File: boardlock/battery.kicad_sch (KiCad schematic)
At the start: 4 parts, among them U4 BQ27441DRZR-G1A, U5 BQ24075RGT

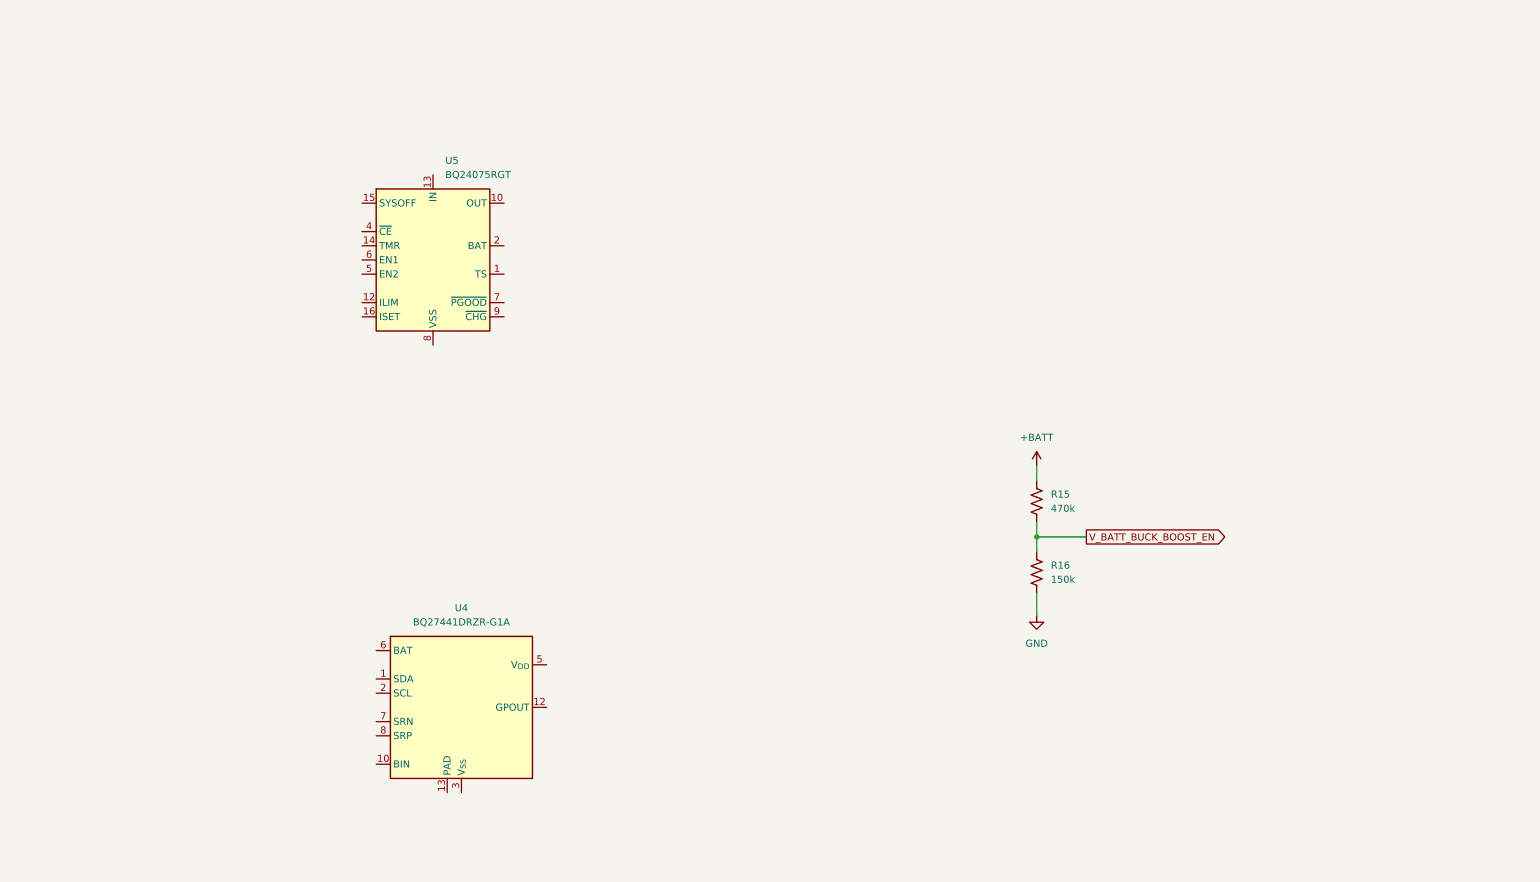
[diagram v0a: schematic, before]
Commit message: Started adding topology for batt charger
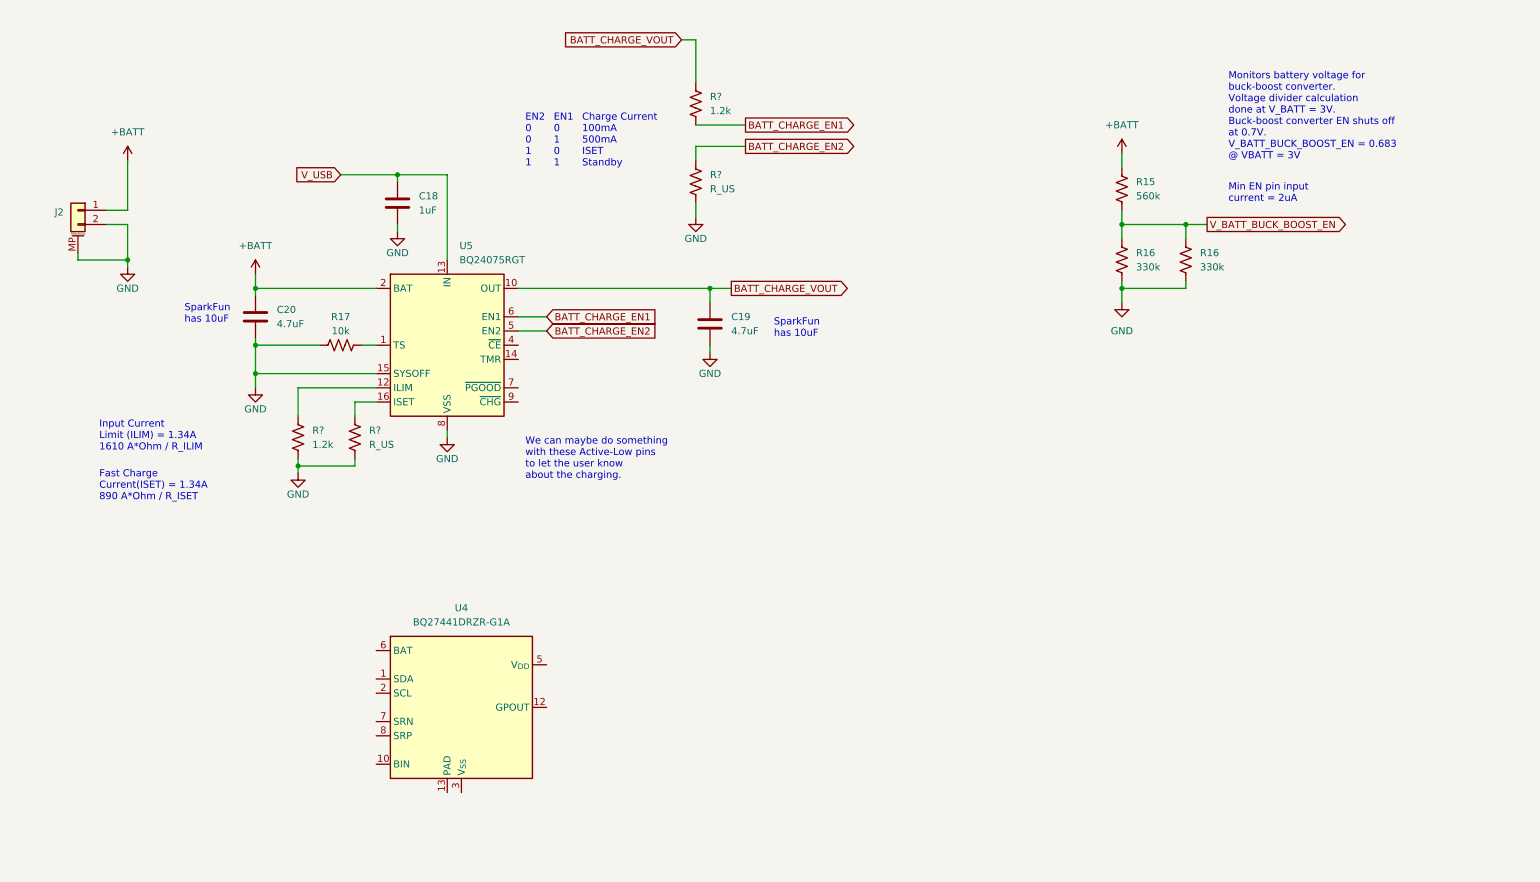
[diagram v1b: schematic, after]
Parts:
- added C18: 1uF, symbol Device:C
- added C19, C20: 4.7uF, symbol Device:C
- added J2: Conn_01x02_MountingPin, symbol Connector_Generic_MountingPin:Conn_01x02_MountingPin
- added R16: 330k, symbol Device:R_US
- added R17: 10k, symbol Device:R_US
- added R? (x2): R_US, symbol Device:R_US
- added R? (x2): 1.2k, symbol Device:R_US
- R15: value 470k -> 560k
- R16: value 150k -> 330k
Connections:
- net +BATT: now also U5.2 (BAT), U5.3 (BAT), C20.1, J2.1 (Pin_1)
- net GND: now also U5.15 (SYSOFF), U5.17 (VSS), U5.8 (VSS), C18.2, C19.2, C20.2, J2.2 (Pin_2), J2.MP (MountPin), R16.2, R17.1, R?.2, R?.2, R?.2
- net V_BATT_BUCK_BOOST_EN: now also R16.1
- net at U5.1 (TS): now also R17.2
- net BATT_CHARGE_VOUT: now reaches U5.10 (OUT), U5.11 (OUT)
- net BATT_CHARGE_VOUT: now also C19.1, R?.1
- net at U5.12 (ILIM): now also R?.1
- net V_USB: now reaches U5.13 (IN)
- net V_USB: now also C18.1
- net at U5.16 (ISET): now also R?.1
- net BATT_CHARGE_EN2: now reaches U5.5 (EN2)
- net BATT_CHARGE_EN2: now also R?.1
- net BATT_CHARGE_EN1: now reaches U5.6 (EN1)
- net BATT_CHARGE_EN1: now also R?.2
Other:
- note added: "Charge Current 100mA 500mA ISET Standby"
- note added: "EN1 0 1 0 1"
- note added: "EN2 0 0 1 1"
- note added: "Fast Charge Current(ISET) = 1.34A 890 A*Ohm / R_ISET"
- note added: "Input Current Limit (ILIM) = 1.34A 1610 A*Ohm / R_ILIM"
- note added: "Min EN pin input current = 2uA"
- note added: "Monitors battery voltage for buck-boost converter. Voltage divider calculation done at V_BATT = 3V. Buck-boost converter EN shuts off at 0.7V. V_BATT_BUCK_BOOST_EN = 0.683 @ VBATT = 3V"
- note added: "SparkFun has 10uF"
- note added: "We can maybe do something with these Active-Low pins to let the user know about the charging."
- moved on the sheet: R15, R16, U5

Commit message: edited battery management
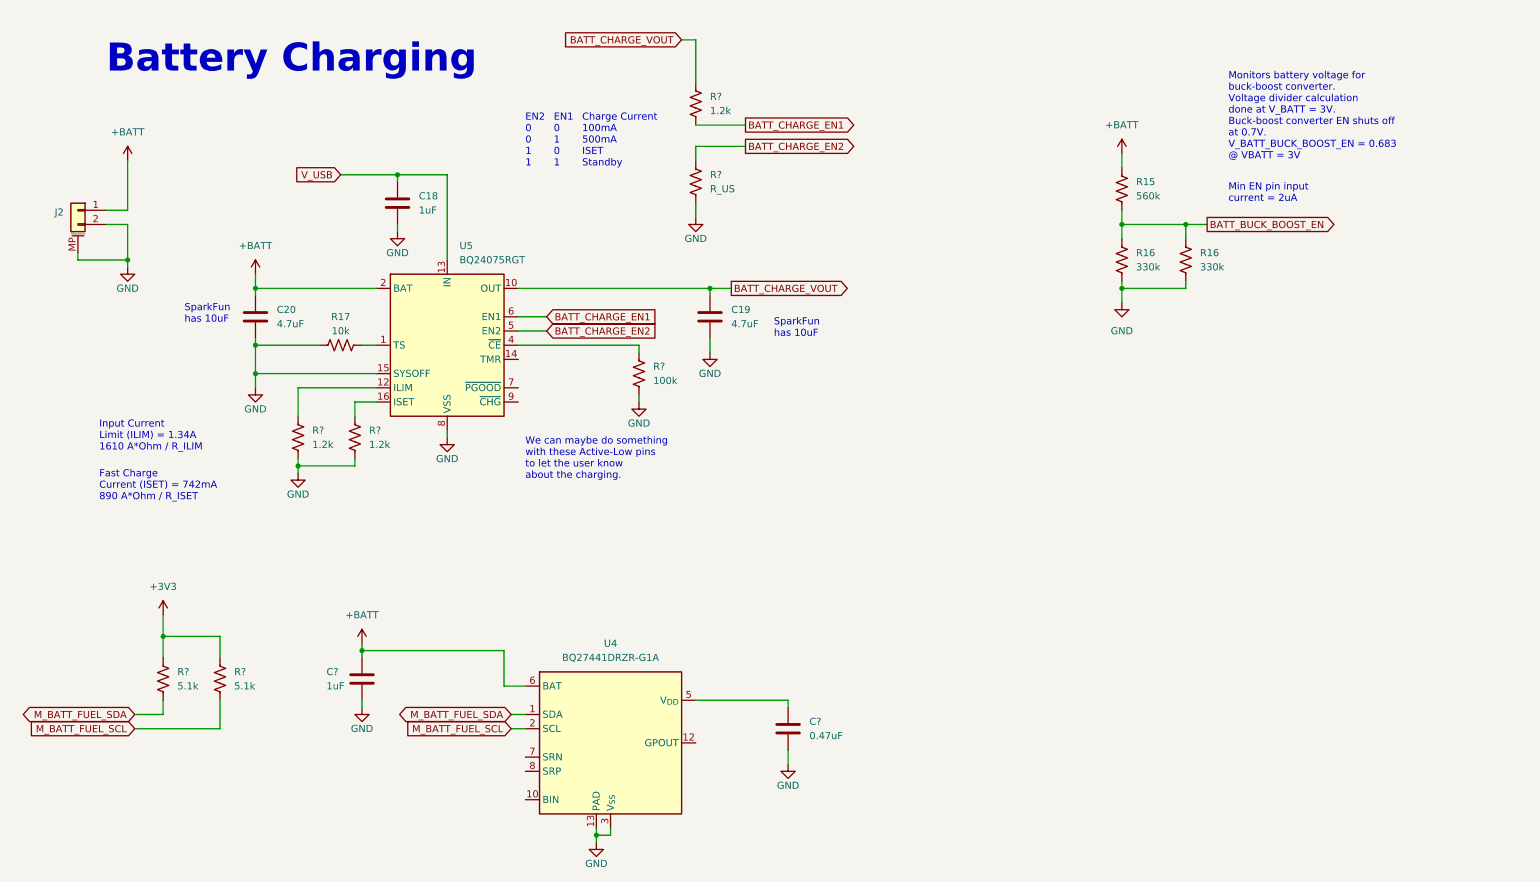
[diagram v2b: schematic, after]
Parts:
- added C?: 0.47uF, symbol Device:C
- added C?: 1uF, symbol Device:C
- added R? (x2): 5.1k, symbol Device:R_US
- added R?: 100k, symbol Device:R_US
- R?: value R_US -> 1.2k
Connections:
- net +BATT: now also U4.6 (BAT), C?.1
- net GND: now also U4.13 (PAD), U4.3 (V_{SS}), C?.2, C?.2, R?.2
- net at U5.4 (~{CE}): now also R?.1
- net M_BATT_FUEL_SDA: now reaches U4.1 (SDA)
- net M_BATT_FUEL_SDA: now also R?.2
- net M_BATT_FUEL_SCL: now reaches U4.2 (SCL)
- net M_BATT_FUEL_SCL: now also R?.2
- net at U4.5 (V_{DD}): now also C?.1
- net V_BATT_BUCK_BOOST_EN renamed BATT_BUCK_BOOST_EN
- new net +3V3: R?.1, R?.1
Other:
- note added: "Battery Charging"
- note added: "Fast Charge Current (ISET) = 742mA 890 A*Ohm / R_ISET"
- note removed: "Fast Charge Current(ISET) = 1.34A 890 A*Ohm / R_ISET"
- moved on the sheet: C19, U4

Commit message: Zecong edits
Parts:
- removed R15: 560k, symbol Device:R_US
- removed R16 (x2): 330k, symbol Device:R_US
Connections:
- net BATT_CHARGE_N_PGOOD: now reaches U5.7 (~{PGOOD})
- net BATT_CHARGE_N_CHG: now reaches U5.9 (~{CHG})
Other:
- note removed: "Min EN pin input current = 2uA"
- note removed: "Monitors battery voltage for buck-boost converter. Voltage divider calculation done at V_BATT = 3V. Buck-boost converter EN shuts off at 0.7V. V_BATT_BUCK_BOOST_EN = 0.683 @ VBATT = 3V"
- moved on the sheet: C?, R?

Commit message: More zecong edits
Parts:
- removed R17: 10k, symbol Device:R_US
- removed R? (x2): 5.1k, symbol Device:R_US
- added R?: 10k, symbol Device:R_US
- added R? (x2): 5.1k, symbol Device:R_US
- added R?: 47k, symbol Device:R_US
- added R?: R_US, symbol Device:R_US
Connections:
- net +3V3: now also R?.1, R?.1
- net +BATT: now also U4.7 (SRN), U4.8 (SRP), R?.1, R?.2
- net GND: now also R?.2, R?.2
- net TS_RESISTOR: now reaches U5.1 (TS)
- net TS_RESISTOR: now also U4.10 (BIN), R?.1
- net at U5.14 (TMR): now also R?.1
- net BATT_CHARGE_N_CHG renamed M_BATT_CHARGE_N_CHG
- net M_BATT_CHARGE_N_CHG: now also R?.2
- net BATT_CHARGE_N_PGOOD renamed M_BATT_CHARGE_N_PGOOD
- net M_BATT_CHARGE_N_PGOOD: now also R?.2
- net M_BATT_FUEL_SCL renamed M_I2C_SCL
- net M_BATT_FUEL_SDA renamed M_I2C_SDA
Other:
- note added: "10k Resistor used in place of 10k NTC thermistor of the battery pack"
- note added: "Need to have connector with BATTERY_IN. This is the input to the shunt resistor. VBATT is the actual battery voltage we want to work with. No sweat on the shunt resistor value. Max voltage drop is 20mV."
- company: (none) -> Schetmatic
- title: (none) -> BoardLock Schematic
- moved on the sheet: C19, C?, R?

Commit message: finishing touches
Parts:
- removed R?: R_US, symbol Device:R_US
- added R?: R_US, symbol Device:R_US
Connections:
- net +BATT: now also R?.1; no longer C?.1, U4.6 (BAT), U4.8 (SRP)
- net M_FUEL_GPOUT: now reaches U4.12 (GPOUT)
- new net BATTERY_IN: C?.1, R?.2, U4.6 (BAT), U4.8 (SRP)
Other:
- note added: "1V8 Internal VDD. Do not use for anything"
- note added: "BATTERY_IN is the input to the shunt resistor. VBATT is the actual battery voltage we want to work with. No sweat on the shunt resistor value. Max voltage drop is 20mV."
- note added: "Need to add to micro sheet"
- note removed: "Need to have connector with BATTERY_IN. This is the input to the shunt resistor. VBATT is the actual battery voltage we want to work with. No sweat on the shunt resistor value. Max voltage drop is 20mV."
- moved on the sheet: C?, U4

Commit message: saving
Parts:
- C19, C20: value 4.7uF -> 10uF
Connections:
- net +BATT: no longer J2.1 (Pin_1)
- net BATTERY_IN: now also J2.1 (Pin_1)
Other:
- note added: "+Batt is the battery voltage after the coloumb shunt resistor"
- note added: "Battery Input"
- note added: "Datasheet has 4.7uF SparkFun has 10uF"
- note added: "Fuel Gauge"
- note removed: "SparkFun has 10uF"
- moved on the sheet: J2
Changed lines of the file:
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@@
   (junction (at 121.92 97.79) (diameter 0) (color 0 0 0 0)
   )
-  (junction (at 35.56 60.96) (diameter 0) (color 0 0 0 0)
+  (junction (at 59.69 151.13) (diameter 0) (color 0 0 0 0)
   )
   (junction (at 213.36 152.4) (diameter 0) (color 0 0 0 0)
@@
     (stroke (width 0) (type default))
   )
-  (wire (pts (xy 35.56 52.07) (xy 35.56 43.18))
-    (stroke (width 0) (type default))
-  )
   (wire (pts (xy 73.66 45.72) (xy 83.82 45.72))
     (stroke (width 0) (type default))
@@
     (stroke (width 0) (type default))
   )
-  (wire (pts (xy 31.75 54.61) (xy 35.56 54.61))
+  (wire (pts (xy 55.88 144.78) (xy 59.69 144.78))
     (stroke (width 0) (type default))
   )
@@
     (stroke (width 0) (type default))
   )
-  (wire (pts (xy 26.67 59.69) (xy 26.67 60.96))
+  (wire (pts (xy 50.8 149.86) (xy 50.8 151.13))
     (stroke (width 0) (type default))
   )
@@
     (stroke (width 0) (type default))
   )
-  (wire (pts (xy 26.67 60.96) (xy 35.56 60.96))
+  (wire (pts (xy 50.8 151.13) (xy 59.69 151.13))
     (stroke (width 0) (type default))
   )
@@
     (stroke (width 0) (type default))
   )
-  (wire (pts (xy 35.56 54.61) (xy 35.56 60.96))
-    (stroke (width 0) (type default))
-  )
-  (wire (pts (xy 31.75 52.07) (xy 35.56 52.07))
+  (wire (pts (xy 59.69 144.78) (xy 59.69 151.13))
+    (stroke (width 0) (type default))
+  )
+  (wire (pts (xy 55.88 142.24) (xy 59.69 142.24))
     (stroke (width 0) (type default))
   )
@@
     (stroke (width 0) (type default))
   )
-  (wire (pts (xy 35.56 60.96) (xy 35.56 62.23))
+  (wire (pts (xy 59.69 151.13) (xy 59.69 152.4))
     (stroke (width 0) (type default))
   )
@@
     (stroke (width 0) (type default))
   )
+  (text "Battery Input" (at 35.56 134.62 0)
+    (effects (font (size 5 5) (thickness 1) bold) (justify left bottom))
+  )
   (text "Need to add to \nmicro sheet" (at 234.95 124.46 0)
+    (effects (font (size 1.27 1.27)) (justify left bottom))
+  )
+  (text "+Batt is the battery\nvoltage after the\ncoloumb shunt resistor"
+    (at 167.64 110.49 0)
+    (effects (font (size 1.27 1.27)) (justify left bottom))
+  )
+  (text "+Batt is the battery\nvoltage after the\ncoloumb shunt resistor"
+    (at 27.94 62.23 0)
     (effects (font (size 1.27 1.27)) (justify left bottom))
   )
@@
     (effects (font (size 1.27 1.27)) (justify left bottom))
   )
+  (text "Fuel Gauge" (at 194.31 102.87 0)
+    (effects (font (size 5 5) (thickness 1) bold) (justify left bottom))
+  )
   (text "Fast Charge\nCurrent (ISET) = 742mA\n890 A*Ohm / R_ISET "
     (at 30.48 104.14 0)
     (effects (font (size 1.27 1.27)) (justify left bottom))
   )
+  (text "Datasheet \nhas 4.7uF\nSparkFun has\n10uF" (at 156.21 78.74 0)
+    (effects (font (size 1.27 1.27)) (justify left bottom))
+  )
   (text "EN1\n0\n1\n0\n1" (at 111.76 44.45 0)
     (effects (font (size 1.27 1.27)) (justify left bottom))
@@
     (effects (font (size 1.27 1.27)) (justify left bottom))
   )
-  (text "SparkFun \nhas 10uF" (at 45.72 72.39 0)
+  (text "Datasheet \nhas 4.7uF\nSparkFun has\n10uF" (at 39.37 77.47 0)
     (effects (font (size 1.27 1.27)) (justify left bottom))
   )
@@
   (text "Input Current\nLimit (ILIM) = 1.34A\n1610 A*Ohm / R_ILIM "
     (at 30.48 95.25 0)
-    (effects (font (size 1.27 1.27)) (justify left bottom))
-  )
-  (text "SparkFun \nhas 10uF" (at 154.94 74.93 0)
     (effects (font (size 1.27 1.27)) (justify left bottom))
   )
@@
     )
   )
+  (global_label "BATTERY_IN" (shape output) (at 59.69 142.24 0) (fields_autoplaced)
+    (effects (font (size 1.27 1.27)) (justify left))
+    (property "Intersheetrefs" "${INTERSHEET_REFS}" (at 73.3795 142.24 0)
+      (effects (font (size 1.27 1.27)) (justify left) hide)
+    )
+  )
   (global_label "M_I2C_SCL" (shape input) (at 198.12 143.51 180) (fields_autoplaced)
     (effects (font (size 1.27 1.27)) (justify right))
@@
       (effects (font (size 1.27 1.27)) (justify left))
     )
-    (property "Value" "4.7uF" (at 62.23 72.39 0)
+    (property "Value" "10uF" (at 62.23 72.39 0)
       (effects (font (size 1.27 1.27)) (justify left))
     )
@@
       (effects (font (size 1.27 1.27)) (justify left))
     )
-    (property "Value" "4.7uF" (at 147.32 72.39 0)
+    (property "Value" "10uF" (at 147.32 72.39 0)
       (effects (font (size 1.27 1.27)) (justify left))
     )
@@
     )
   )
-  (symbol (lib_id "power:+BATT") (at 35.56 43.18 0) (mirror y) (unit 1)
-    (in_bom yes) (on_board yes) (dnp no) (fields_autoplaced)
-    (property "Reference" "#PWR032" (at 35.56 46.99 0)
-      (effects (font (size 1.27 1.27)) hide)
-    )
-    (property "Value" "+BATT" (at 35.56 38.1 0)
-      (effects (font (size 1.27 1.27)))
-    )
-    (property "Footprint" "" (at 35.56 43.18 0)
-      (effects (font (size 1.27 1.27)) hide)
-    )
-    (property "Datasheet" "" (at 35.56 43.18 0)
-      (effects (font (size 1.27 1.27)) hide)
-    )
-    (pin "1")
-    (instances
-      (project "boardlock"
-        (path "/e1fc29ce-837e-4062-84d8-c7e423f9eab9/5801071c-337d-449a-92e5-5afeb5febc0d"
-          (reference "#PWR032") (unit 1)
-        )
-        (path "/e1fc29ce-837e-4062-84d8-c7e423f9eab9/a05f4dcd-7a18-4529-a05e-43353e81fbf8"
-          (reference "#PWR034") (unit 1)
-        )
-      )
-    )
-  )
-  (symbol (lib_id "Connector_Generic_MountingPin:Conn_01x02_MountingPin") (at 26.67 52.07 0) (mirror y) (unit 1)
+  (symbol (lib_id "Connector_Generic_MountingPin:Conn_01x02_MountingPin") (at 50.8 142.24 0) (mirror y) (unit 1)
     (in_bom yes) (on_board yes) (dnp no)
-    (property "Reference" "J2" (at 24.13 52.4256 0)
-      (effects (font (size 1.27 1.27)) (justify left))
-    )
-    (property "Value" "Conn_01x02_MountingPin" (at 24.13 54.9656 90)
+    (property "Reference" "J2" (at 48.26 142.5956 0)
+      (effects (font (size 1.27 1.27)) (justify left))
+    )
+    (property "Value" "Conn_01x02_MountingPin" (at 48.26 145.1356 90)
       (effects (font (size 1.27 1.27)) (justify right) hide)
     )
-    (property "Footprint" "" (at 26.67 52.07 0)
-      (effects (font (size 1.27 1.27)) hide)
-    )
-    (property "Datasheet" "~" (at 26.67 52.07 0)
+    (property "Footprint" "" (at 50.8 142.24 0)
+      (effects (font (size 1.27 1.27)) hide)
+    )
+    (property "Datasheet" "~" (at 50.8 142.24 0)
       (effects (font (size 1.27 1.27)) hide)
     )
@@
     )
   )
-  (symbol (lib_id "power:GND") (at 35.56 62.23 0) (mirror y) (unit 1)
+  (symbol (lib_id "power:GND") (at 59.69 152.4 0) (mirror y) (unit 1)
     (in_bom yes) (on_board yes) (dnp no)
-    (property "Reference" "#PWR035" (at 35.56 68.58 0)
-      (effects (font (size 1.27 1.27)) hide)
-    )
-    (property "Value" "GND" (at 35.56 66.04 0)
+    (property "Reference" "#PWR035" (at 59.69 158.75 0)
+      (effects (font (size 1.27 1.27)) hide)
+    )
+    (property "Value" "GND" (at 59.69 156.21 0)
       (effects (font (size 1.27 1.27)))
     )
-    (property "Footprint" "" (at 35.56 62.23 0)
-      (effects (font (size 1.27 1.27)) hide)
-    )
-    (property "Datasheet" "" (at 35.56 62.23 0)
-      (effects (font (size 1.27 1.27)) hide)
-    )
+    (property "Footprint" "" (at 59.69 152.4 0)
+      (effects (font (size 1.27 1.27)) hide)
+    )
+    (property "Datasheet" "" (at 59.69 152.4 0)
+      (effects (font (size 1.27 1.27)) hide)
+    )
